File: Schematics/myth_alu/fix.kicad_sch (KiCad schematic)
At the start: 5 parts, among them U18 4075, U19 74HC157, U20 74HC283, U21 74HC283, U22 74AHC574

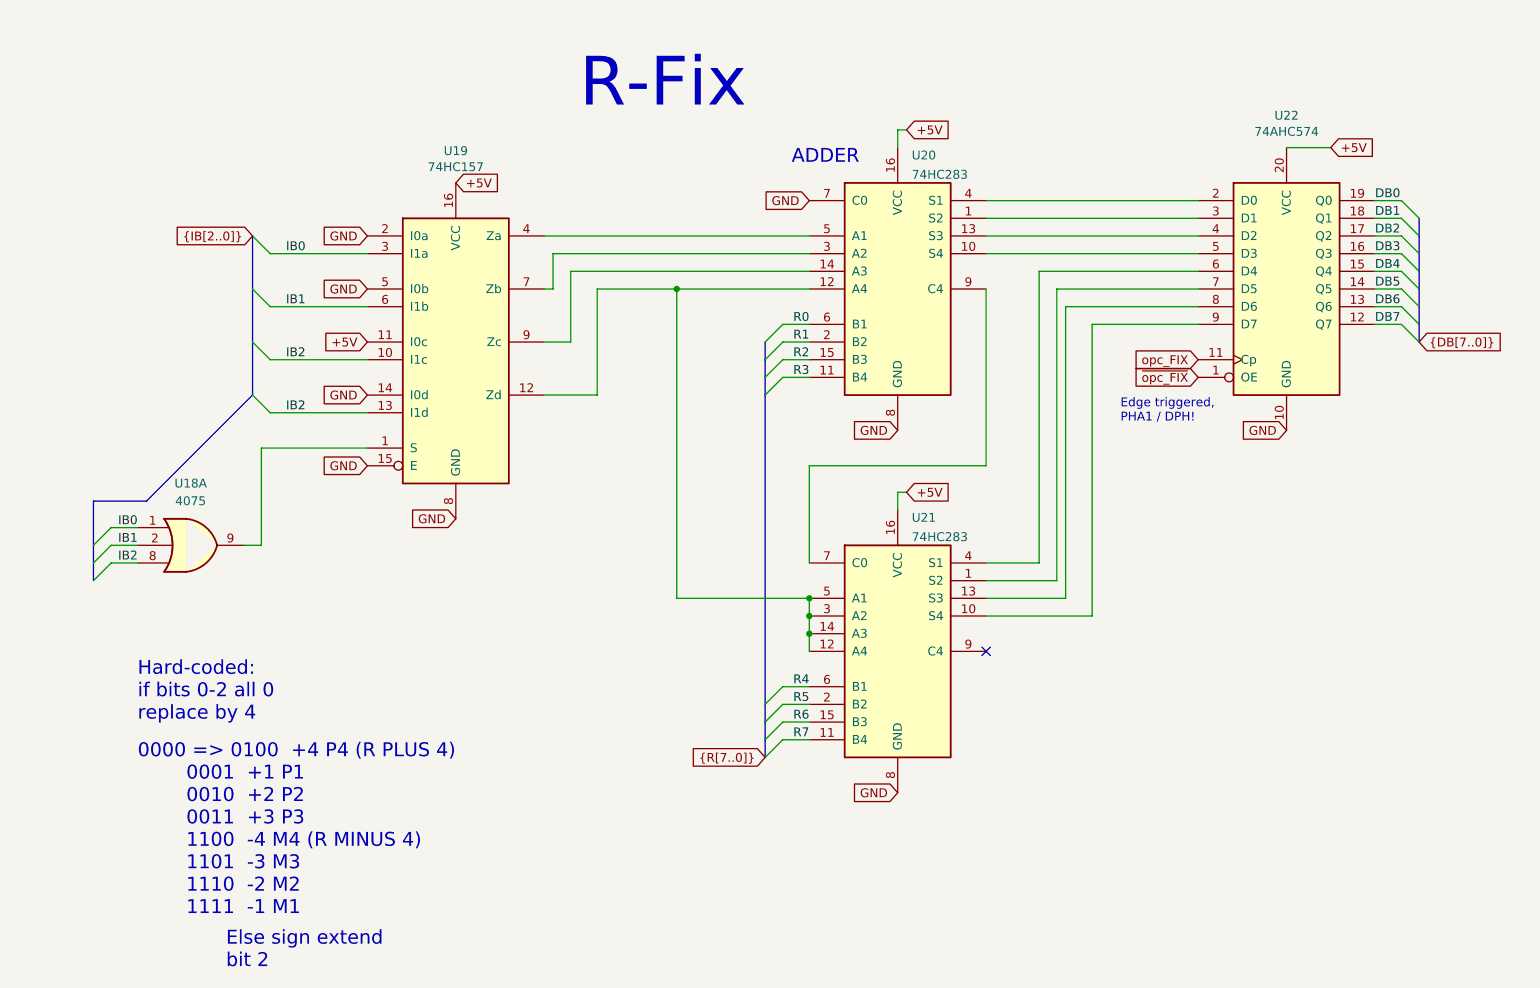
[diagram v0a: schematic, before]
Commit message: Change d to g
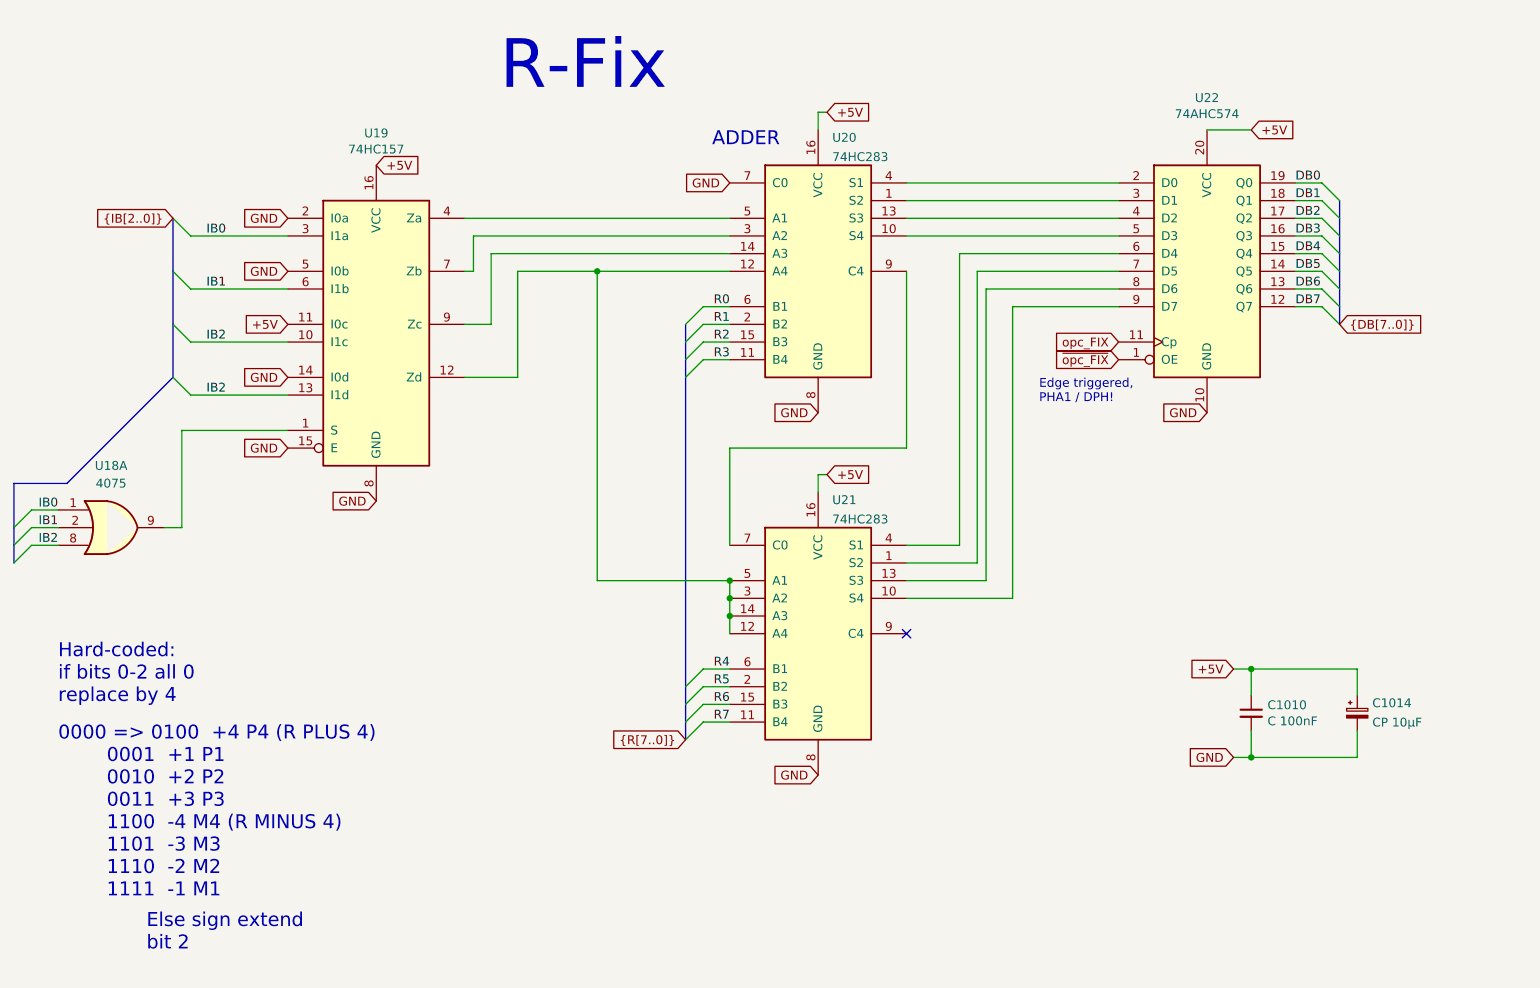
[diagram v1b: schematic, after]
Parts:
- added C1010: C 100nF, Capacitor_THT:C_Disc_D5.0mm_W2.5mm_P2.50mm, symbol Device:C_Small
- added C1014: CP 10μF, Capacitor_THT:CP_Radial_D6.3mm_P2.50mm, symbol Device:C_Polarized_Small
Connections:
- net +5V: now also C1010.1, C1014.1
- net GND: now also C1010.2, C1014.2
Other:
- moved on the sheet: U18A, U19, U20, U21, U22
